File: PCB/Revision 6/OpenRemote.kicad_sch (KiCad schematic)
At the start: 180 parts, among them J1 USB_C_Receptacle_USB2.0, J2 Conn_01x50, J3 JST_PH_B2B-PH, J4 2.54x2 Header, J5 Micro_SD_Card, J6 ER-CON06HB-1_TOUCH, J7 JST_PH_B2B-PH, Q1 DMG2301L, Q2 MBT3904DW1, Q3 DMG2301L, Q4 DMG2301L, Q5 DMG2301L, Q6 FS8205A, Q7 DMG2301L, U1 DW01A, U10 APX803S, U11 TP4056, U12 TCA8418, U2 XC6220B331, U3 CH340C, U4 USBLC6-2P6, U5 LIS3DHTR, U6 TSSP77038, U7 ESP32-S3-WROOM-1-N16R8, U8 AP2112K-3.3, U9 MAX17048G

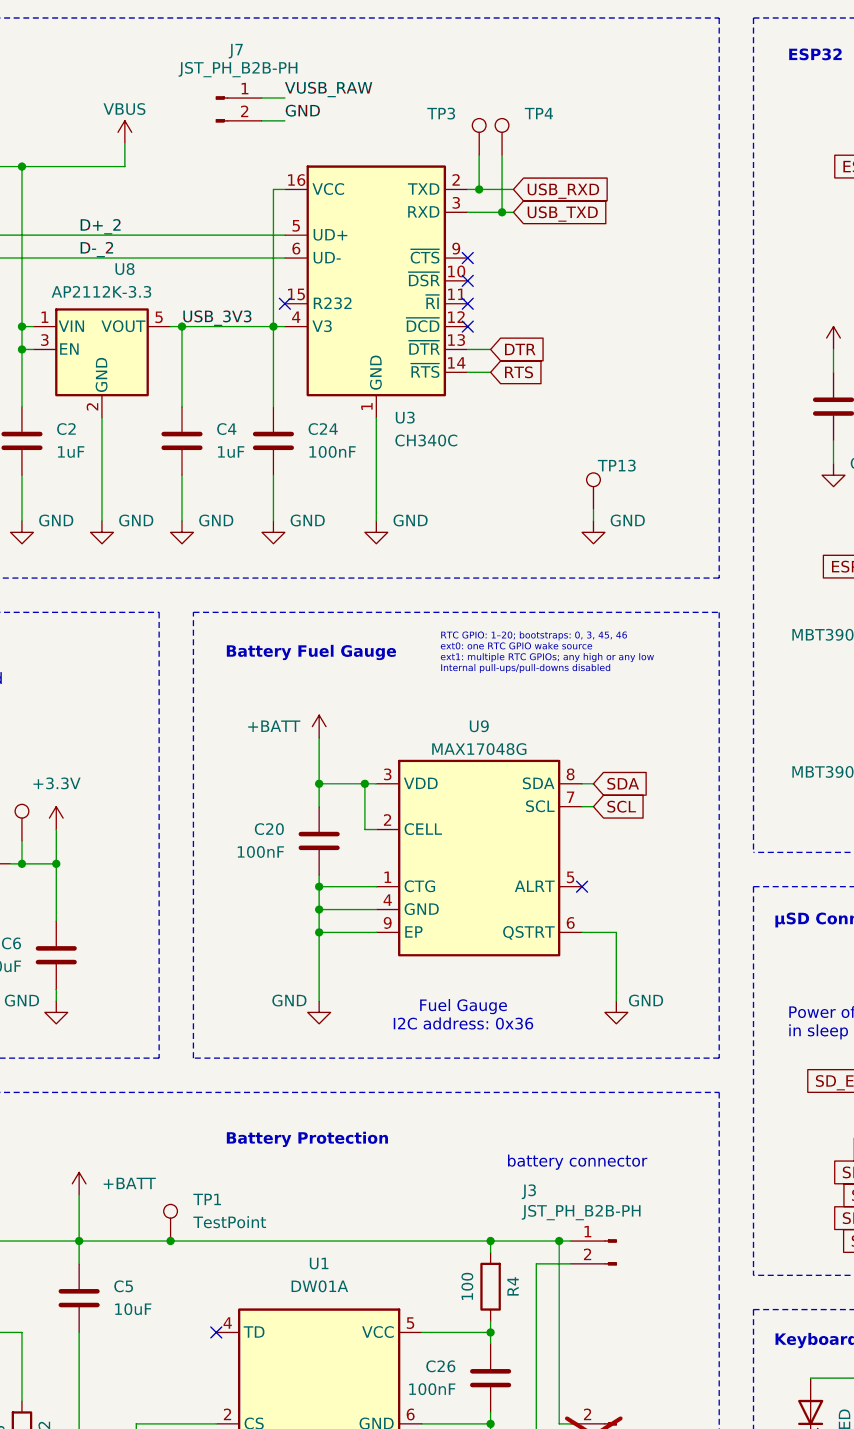
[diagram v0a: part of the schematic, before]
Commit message: Sync Rev 6 hardware work from workstation
PCB (Revision 6):
- J3 battery connector polarity update; the old KiBuzzard "(+)(-)"
  silkscreen graphic is replaced by a plain "Battery" F.Silkscreen label
- J3 nudged 0.1 mm in X
- Regenerated gerber.zip from the current board (kicad-cli 10.0.4)
- U5 (LIS3DHTR) now marked DNP; C14/C27/U10 added as DNP
- CPL.csv and BOM.xlsx left as-is pending regeneration

Also adds previously unpublished work from the workstation: Case Rev6
and Dock Rev6 CAD, Fusion scripts, PCB imports, Dock Rev6 board and
scripts, and Rev6 render images.

Co-Authored-By: Claude Opus 5 <noreply@anthropic.com>
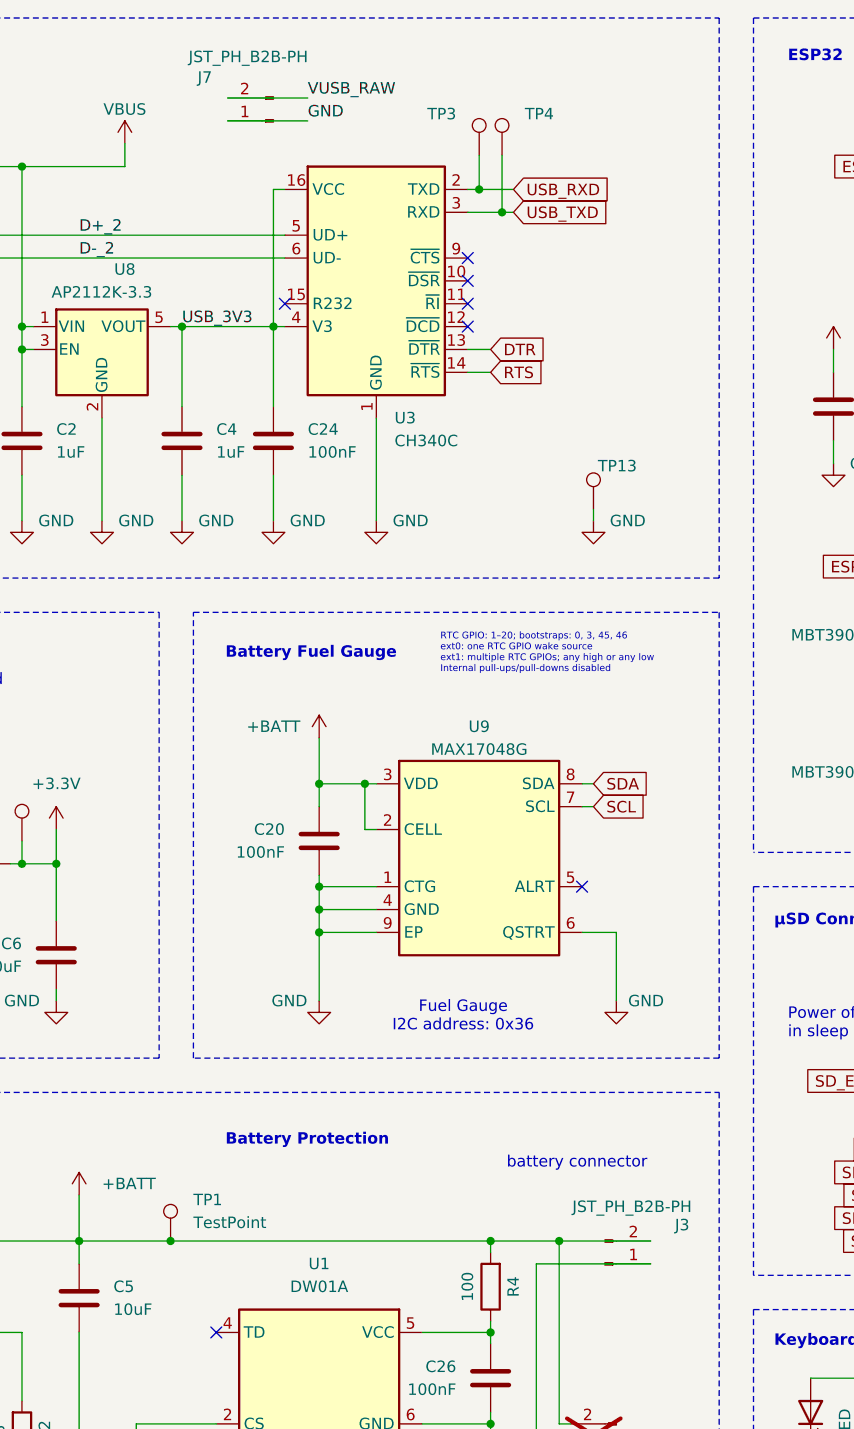
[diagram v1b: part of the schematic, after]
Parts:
- D1: LCSC C155590 -> C49238173
- MIC1: now left out of the parts list
- R21: LCSC C2849062 -> C313912
- R45, R46, R47: LCSC (none) -> C23162
- R8: LCSC C99782 -> C22765
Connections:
- net +BATT: now also J3.2 (Pin_2); no longer J3.1 (Pin_1)
- net -BATT: now also J3.1 (Pin_1); no longer J3.2 (Pin_2)
- net GND: now also J7.1 (Pin_1); no longer J7.2 (Pin_2)
- net VUSB_RAW: now also J7.2 (Pin_2); no longer J7.1 (Pin_1)
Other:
- moved on the sheet: J3, J7
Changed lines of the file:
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@@
 	)
 	(junction
-		(at 143.51 154.94)
+		(at 151.13 154.94)
 		(diameter 0)
 		(color 0 0 0 0)
@@
 	)
 	(junction
-		(at 151.13 154.94)
-		(diameter 0)
-		(color 0 0 0 0)
-	)
-	(junction
 		(at 354.33 102.87)
 		(diameter 0)
@@
 	)
 	(junction
+		(at 148.59 177.8)
+		(diameter 0)
+		(color 0 0 0 0)
+	)
+	(junction
 		(at 88.9 259.08)
 		(diameter 0)
@@
 	)
 	(junction
-		(at 148.59 177.8)
-		(diameter 0)
-		(color 0 0 0 0)
-	)
-	(junction
 		(at 214.63 170.18)
 		(diameter 0)
@@
 	)
 	(junction
+		(at 143.51 154.94)
+		(diameter 0)
+		(color 0 0 0 0)
+	)
+	(junction
 		(at 30.48 254)
 		(diameter 0)
@@
 	(wire
 		(pts
-			(xy 143.51 154.94) (xy 151.13 154.94)
-		)
-		(stroke
-			(width 0)
-			(type default)
-		)
-	)
-	(wire
-		(pts
 			(xy 83.82 165.1) (xy 91.44 165.1)
 		)
@@
 	(wire
 		(pts
-			(xy 152.4 157.48) (xy 148.59 157.48)
-		)
-		(stroke
-			(width 0)
-			(type default)
-		)
-	)
-	(wire
-		(pts
 			(xy 264.16 63.5) (xy 266.7 63.5)
 		)
@@
 	(wire
 		(pts
+			(xy 151.13 154.94) (xy 161.29 154.94)
+		)
+		(stroke
+			(width 0)
+			(type default)
+		)
+	)
+	(wire
+		(pts
+			(xy 151.13 154.94) (xy 151.13 175.26)
+		)
+		(stroke
+			(width 0)
+			(type default)
+		)
+	)
+	(wire
+		(pts
 			(xy 52.07 63.5) (xy 52.07 66.04)
 		)
@@
 	(wire
 		(pts
-			(xy 151.13 154.94) (xy 152.4 154.94)
-		)
-		(stroke
-			(width 0)
-			(type default)
-		)
-	)
-	(wire
-		(pts
 			(xy 58.42 149.86) (xy 58.42 154.94)
 		)
@@
 	(wire
 		(pts
+			(xy 114.3 27.94) (xy 123.19 27.94)
+		)
+		(stroke
+			(width 0)
+			(type default)
+		)
+	)
+	(wire
+		(pts
 			(xy 381 146.05) (xy 381 148.59)
 		)
@@
 	(wire
 		(pts
+			(xy 143.51 154.94) (xy 151.13 154.94)
+		)
+		(stroke
+			(width 0)
+			(type default)
+		)
+	)
+	(wire
+		(pts
 			(xy 43.18 232.41) (xy 43.18 241.3)
 		)
@@
 	(wire
 		(pts
-			(xy 118.11 27.94) (xy 120.65 27.94)
-		)
-		(stroke
-			(width 0)
-			(type default)
-		)
-	)
-	(wire
-		(pts
 			(xy 209.55 220.98) (xy 224.79 220.98)
 		)
@@
 	(wire
 		(pts
+			(xy 114.3 30.48) (xy 123.19 30.48)
+		)
+		(stroke
+			(width 0)
+			(type default)
+		)
+	)
+	(wire
+		(pts
 			(xy 351.79 90.17) (xy 365.76 90.17)
 		)
@@
 	(wire
 		(pts
-			(xy 118.11 30.48) (xy 120.65 30.48)
-		)
-		(stroke
-			(width 0)
-			(type default)
-		)
-	)
-	(wire
-		(pts
 			(xy 104.14 241.3) (xy 104.14 250.19)
 		)
@@
 	(wire
 		(pts
+			(xy 148.59 157.48) (xy 148.59 177.8)
+		)
+		(stroke
+			(width 0)
+			(type default)
+		)
+	)
+	(wire
+		(pts
 			(xy 115.57 220.98) (xy 115.57 223.52)
 		)
@@
 	(wire
 		(pts
-			(xy 151.13 154.94) (xy 151.13 175.26)
-		)
-		(stroke
-			(width 0)
-			(type default)
-		)
-	)
-	(wire
-		(pts
 			(xy 209.55 229.87) (xy 209.55 231.14)
 		)
@@
 	(wire
 		(pts
-			(xy 110.49 212.09) (xy 110.49 213.36)
+			(xy 148.59 157.48) (xy 161.29 157.48)
 		)
 		(stroke
@@
 	(wire
 		(pts
-			(xy 148.59 157.48) (xy 148.59 177.8)
+			(xy 110.49 212.09) (xy 110.49 213.36)
 		)
 		(stroke
@@
 	)
 	(label "VUSB_RAW"
-		(at 120.65 27.94 0)
+		(at 123.19 27.94 0)
 		(effects
 			(font
@@
 	)
 	(label "GND"
-		(at 120.65 30.48 0)
+		(at 123.19 30.48 0)
 		(effects
 			(font
@@
 		(in_bom no)
 		(on_board yes)
-		(in_pos_files yes)
+		(in_pos_files no)
 		(dnp no)
 		(fields_autoplaced yes)
@@
 		(body_style 1)
 		(exclude_from_sim no)
-		(in_bom yes)
+		(in_bom no)
 		(on_board yes)
-		(in_pos_files yes)
+		(in_pos_files no)
 		(dnp no)
 		(property "Reference" "MIC1"
@@
 			)
 		)
-		(property "LCSC" ""
+		(property "LCSC" "C23162"
 			(at 260.35 97.79 0)
 			(hide yes)
@@
 			)
 		)
-		(property "LCSC" "C2849062"
+		(property "LCSC" "C313912"
 			(at 209.55 226.06 0)
 			(hide yes)
@@
 		(in_bom no)
 		(on_board yes)
-		(in_pos_files yes)
+		(in_pos_files no)
 		(dnp no)
 		(fields_autoplaced yes)
@@
 			)
 		)
-		(property "LCSC" "C99782"
+		(property "LCSC" "C22765"
 			(at 91.44 176.53 0)
 			(hide yes)
@@
 	(symbol
 		(lib_id "Connector:Conn_01x02_Male")
-		(at 157.48 154.94 0)
-		(mirror y)
+		(at 156.21 157.48 0)
+		(mirror x)
 		(unit 1)
 		(body_style 1)
@@
 		(dnp no)
 		(property "Reference" "J3"
-			(at 147.066 149.352 0)
+			(at 165.608 153.162 0)
 			(show_name no)
 			(do_not_autoplace no)
@@
 		)
 		(property "Value" "JST_PH_B2B-PH"
-			(at 147.066 151.638 0)
+			(at 165.862 151.13 0)
 			(show_name no)
 			(do_not_autoplace no)
@@
 		)
 		(property "Footprint" "OpenRemoteLib:JST_PH_B2B-PH-SM4-TB_1x02-1MP_P2.00mm_Vertical"
-			(at 157.48 154.94 0)
+			(at 156.21 157.48 0)
 			(hide yes)
 			(show_name no)
@@
 		)
 		(property "Datasheet" ""
-			(at 157.48 154.94 0)
+			(at 156.21 157.48 0)
 			(hide yes)
 			(show_name no)
@@
 		)
 		(property "Description" ""
-			(at 157.48 154.94 0)
+			(at 156.21 157.48 0)
 			(hide yes)
 			(show_name no)
@@
 		)
 		(property "LCSC" "C160352"
-			(at 157.48 154.94 0)
+			(at 156.21 157.48 0)
 			(hide yes)
 			(show_name no)
@@
 		(in_bom no)
 		(on_board yes)
-		(in_pos_files yes)
+		(in_pos_files no)
 		(dnp no)
 		(fields_autoplaced yes)
@@
 			)
 		)
-		(property "LCSC" ""
+		(property "LCSC" "C23162"
 			(at 260.35 102.87 0)
 			(hide yes)
@@
 			)
 		)
-		(property "LCSC" ""
+		(property "LCSC" "C23162"
 			(at 260.35 107.95 0)
 			(hide yes)
@@
 		(in_bom no)
 		(on_board yes)
-		(in_pos_files yes)
+		(in_pos_files no)
 		(dnp no)
 		(fields_autoplaced yes)
@@
 	(symbol
 		(lib_id "Connector:Conn_01x02_Male")
-		(at 113.03 27.94 0)
+		(at 119.38 30.48 180)
 		(unit 1)
 		(body_style 1)
@@
 		(dnp no)
 		(property "Reference" "J7"
-			(at 115.316 22.606 0)
+			(at 111.76 25.654 0)
 			(show_name no)
 			(do_not_autoplace no)
@@
 		)
 		(property "Value" "JST_PH_B2B-PH"
-			(at 115.57 24.638 0)
+			(at 116.586 23.368 0)
 			(show_name no)
 			(do_not_autoplace no)
@@
 		)
 		(property "Footprint" "OpenRemoteLib:JST_PH_B2B-PH-SM4-TB_1x02-1MP_P2.00mm_Vertical"
-			(at 113.03 27.94 0)
+			(at 119.38 30.48 0)
 			(hide yes)
 			(show_name no)
@@
 		)
 		(property "Datasheet" ""
-			(at 113.03 27.94 0)
+			(at 119.38 30.48 0)
 			(hide yes)
 			(show_name no)
@@
 		)
 		(property "Description" ""
-			(at 113.03 27.94 0)
+			(at 119.38 30.48 0)
 			(hide yes)
 			(show_name no)
@@
 		)
 		(property "LCSC" "C160352"
-			(at 113.03 27.94 0)
+			(at 119.38 30.48 0)
 			(hide yes)
 			(show_name no)
@@
 			)
 		)
-		(property "LCSC" "C155590"
+		(property "LCSC" "C49238173"
 			(at 46.99 113.03 0)
 			(hide yes)

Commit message: Merge MIC_VDD with IO45 net and regenerate Rev6 gerbers
Schematic:
- Added the missing 10.16 mm wire from (281.94, 69.85) to the MIC_VDD
  global label at (292.10, 69.85). The label had been drawn but never
  landed on the net, so MIC_VDD and Net-(D3-A) were two separate nets
  joined only by a track physically overlapping U7 pad 26 and D3 pad 2.
- MIC_VDD now carries D3.2, MIC1.2 and U7.26 (IO45); Net-(D3-A) is gone.

PCB:
- Netlist re-imported; MIC1 pin 6 grounded via a track to a new GND via
  at (145.50, 104.50) landing in the B.Cu plane; MIC_VDD routed properly.
- DRC errors 51 -> 44: all 4 shorting_items cleared, solder_mask_bridge
  9 -> 4 (remaining four are the fiducials).
- Regenerated gerber.zip from the current board (kicad-cli 10.0.4).
  Changes confined to F.Cu, B.Cu and one new PTH via; silkscreen, mask,
  paste and edge cuts are byte-identical to the previous set.

Also adds Dock Rev6 production files and the pogo-pin case STL.

Known outstanding: 11 clearance violations remain in the J7 5V-in and
J3 battery routing, tightest 0.100 mm, below JLCPCB's 0.127 mm minimum.
CPL.csv and BOM.xlsx are unchanged and still need regeneration.

Co-Authored-By: Claude Opus 5 <noreply@anthropic.com>
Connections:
- net MIC_VDD: now also D3.2 (A), U7.26 (IO45)
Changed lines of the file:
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@@
+	(wire
+		(pts
+			(xy 292.1 69.85) (xy 281.94 69.85)
+		)
+		(stroke
+			(width 0)
+			(type default)
+		)
+	)
 	(wire
 		(pts
